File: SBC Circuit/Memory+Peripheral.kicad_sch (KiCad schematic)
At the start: 19 parts, among them J5 Conn_01x03_Pin, J6 Conn_01x08_Pin, J7 Conn_01x06_Pin, U3 68681, U4 MCM6206CP, U5 MCM6206CP, U6 28C256, U7 28C256, X2 EC11

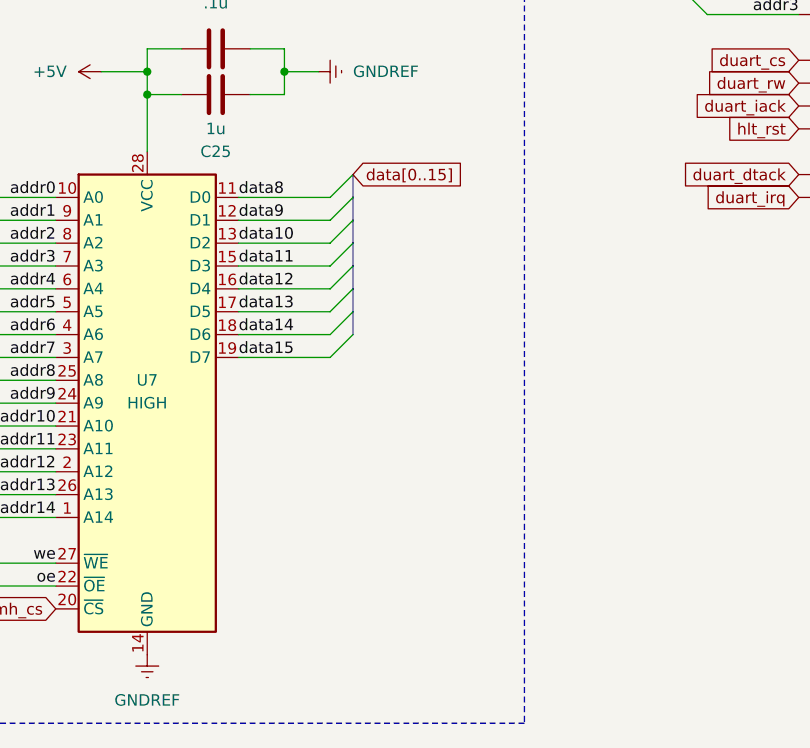
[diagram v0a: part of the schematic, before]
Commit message: Finished wiring ROM High
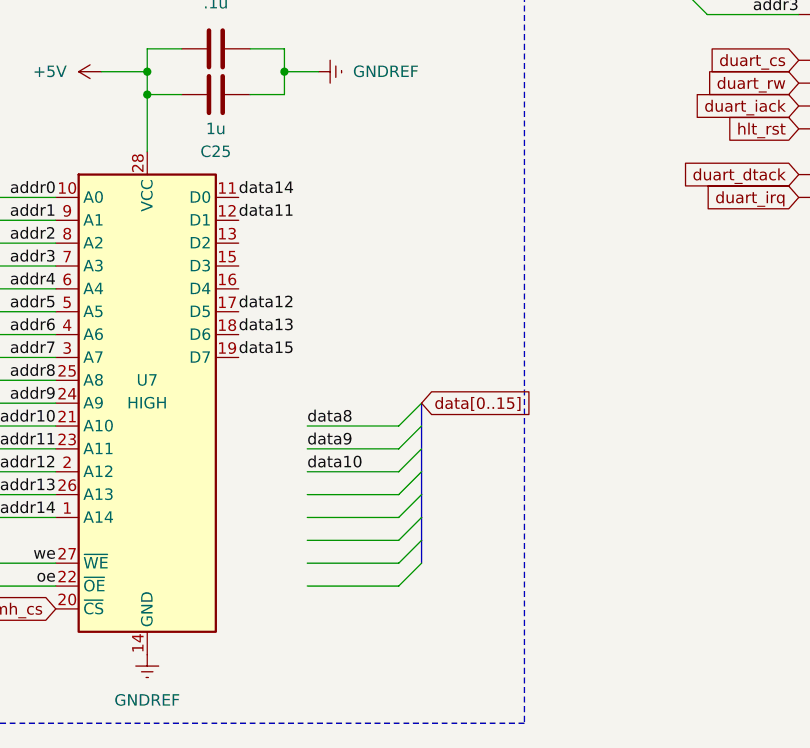
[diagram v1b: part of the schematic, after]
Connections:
- net data10: no longer U7.13 (D2)
- net data11: now also U7.12 (D1); no longer U7.15 (D3)
- net data12: now also U7.17 (D5); no longer U7.16 (D4)
- net data13: now also U7.18 (D6); no longer U7.17 (D5)
- net data14: now also U7.11 (D0); no longer U7.18 (D6)
- net data8: no longer U7.11 (D0)
- net data9: no longer U7.12 (D1)

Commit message: Wire high ROM correctly
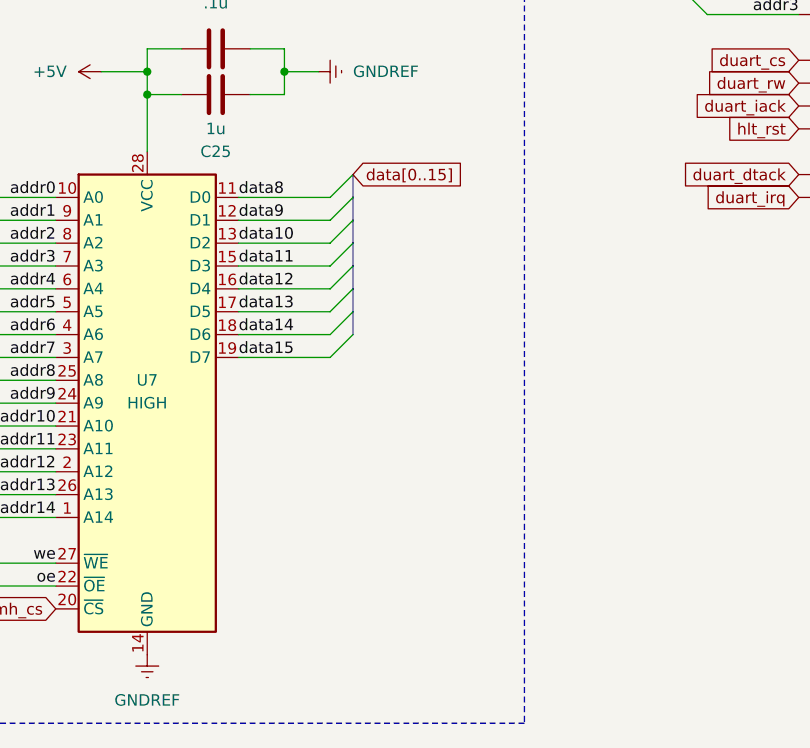
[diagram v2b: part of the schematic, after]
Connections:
- net data10: now also U7.13 (D2)
- net data11: now also U7.15 (D3); no longer U7.12 (D1)
- net data12: now also U7.16 (D4); no longer U7.17 (D5)
- net data13: now also U7.17 (D5); no longer U7.18 (D6)
- net data14: now also U7.18 (D6); no longer U7.11 (D0)
- net data8: now also U7.11 (D0)
- net data9: now also U7.12 (D1)
